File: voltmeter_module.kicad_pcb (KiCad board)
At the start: 2 copper layers, 16 parts, among them K1 EE2-3NUX, Q1 2N7002, U1 REF5030AD, U2 TL072, U3 MCP3561RT-E_ST, U5 ISO7762FDW, U6 NCS21802DMR2G, U7 CD4051B

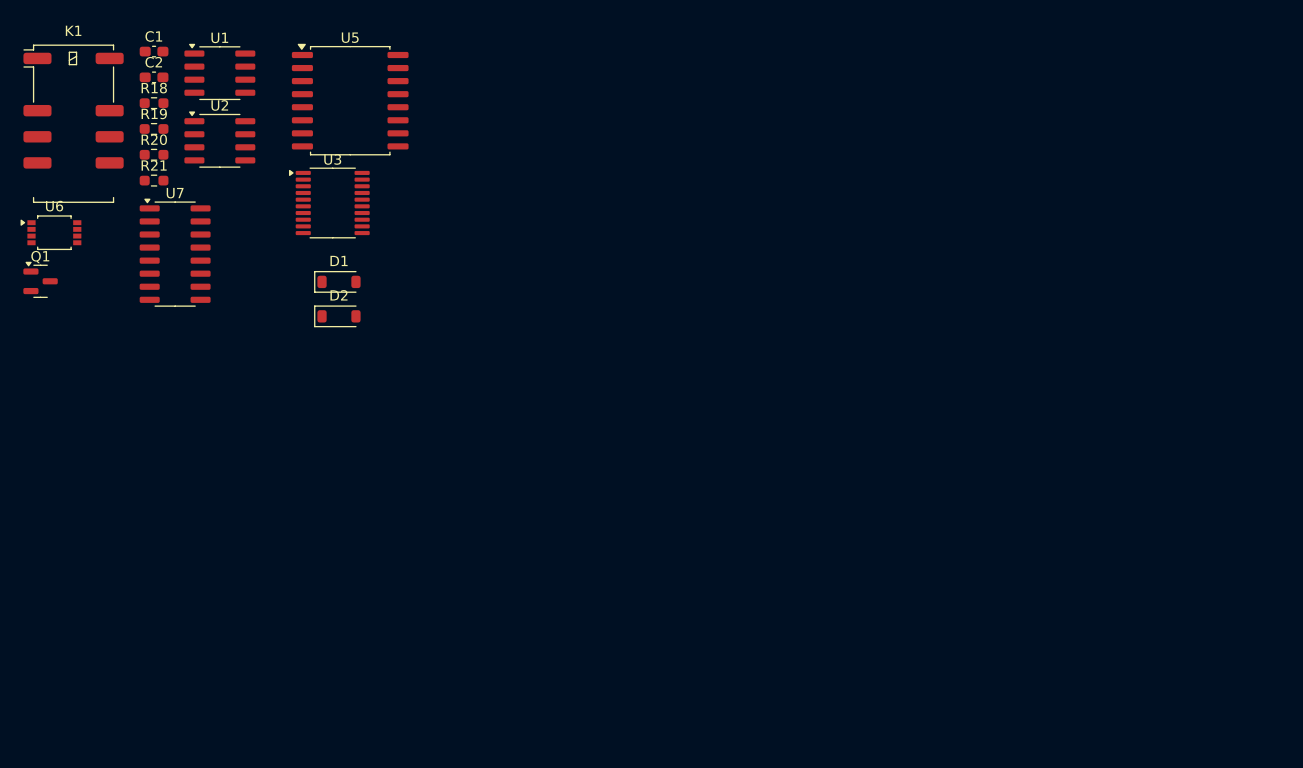
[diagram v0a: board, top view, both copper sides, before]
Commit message: Bootstraped input buffer.
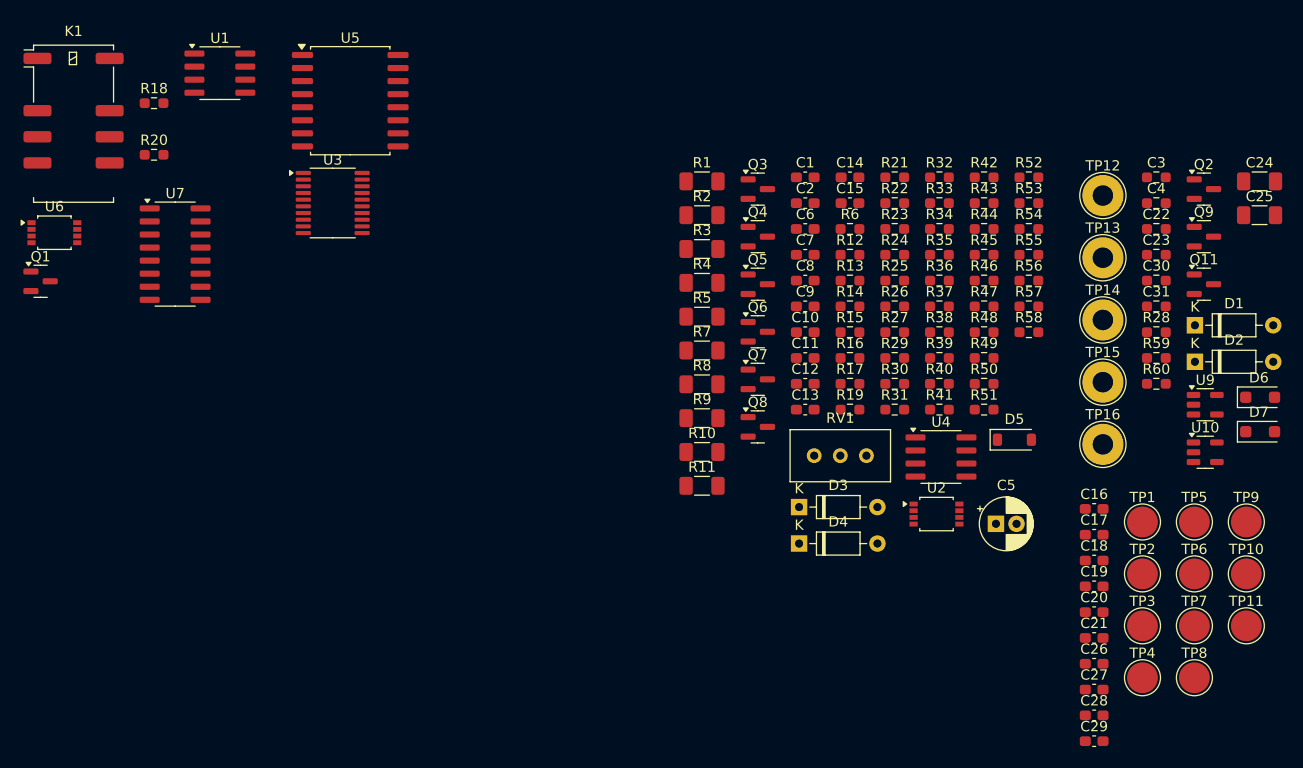
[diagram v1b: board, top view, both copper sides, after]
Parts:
- added C10: 100n, Capacitor_SMD:C_0603_1608Metric_Pad1.08x0.95mm_HandSolder, F.Cu at (184.2, 84.2)
- added C11: 1u, Capacitor_SMD:C_0603_1608Metric_Pad1.08x0.95mm_HandSolder, F.Cu at (184.2, 86.8)
- added C12: 1u, Capacitor_SMD:C_0603_1608Metric_Pad1.08x0.95mm_HandSolder, F.Cu at (184.2, 89.3)
- added C13: 100n, Capacitor_SMD:C_0603_1608Metric_Pad1.08x0.95mm_HandSolder, F.Cu at (184.2, 91.8)
- added C14: 100n, Capacitor_SMD:C_0603_1608Metric_Pad1.08x0.95mm_HandSolder, F.Cu at (188.6, 69.2)
- added C15: 100n, Capacitor_SMD:C_0603_1608Metric_Pad1.08x0.95mm_HandSolder, F.Cu at (188.6, 71.7)
- added C16: 100n, Capacitor_SMD:C_0603_1608Metric_Pad1.08x0.95mm_HandSolder, F.Cu at (212.3, 101.4)
- added C17: 100n, Capacitor_SMD:C_0603_1608Metric_Pad1.08x0.95mm_HandSolder, F.Cu at (212.3, 103.9)
- added C18: 1u, Capacitor_SMD:C_0603_1608Metric_Pad1.08x0.95mm_HandSolder, F.Cu at (212.3, 106.5)
- added C19: 1u, Capacitor_SMD:C_0603_1608Metric_Pad1.08x0.95mm_HandSolder, F.Cu at (212.3, 109.0)
- added C20: 1u, Capacitor_SMD:C_0603_1608Metric_Pad1.08x0.95mm_HandSolder, F.Cu at (212.3, 111.5)
- added C21: 100n, Capacitor_SMD:C_0603_1608Metric_Pad1.08x0.95mm_HandSolder, F.Cu at (212.3, 114.0)
- added C22: 220n, Resistor_SMD:R_0603_1608Metric_Pad0.98x0.95mm_HandSolder, F.Cu at (218.3, 74.2)
- added C23: 220n, Resistor_SMD:R_0603_1608Metric_Pad0.98x0.95mm_HandSolder, F.Cu at (218.3, 76.7)
- added C24: 2u2, Resistor_SMD:R_1206_3216Metric_Pad1.30x1.75mm_HandSolder, F.Cu at (228.4, 69.6)
- added C25: 2u2, Resistor_SMD:R_1206_3216Metric_Pad1.30x1.75mm_HandSolder, F.Cu at (228.4, 72.9)
- added C26: 1u, Capacitor_SMD:C_0603_1608Metric_Pad1.08x0.95mm_HandSolder, F.Cu at (212.3, 116.5)
- added C27: 100n, Capacitor_SMD:C_0603_1608Metric_Pad1.08x0.95mm_HandSolder, F.Cu at (212.3, 119.0)
- added C28: 1u, Capacitor_SMD:C_0603_1608Metric_Pad1.08x0.95mm_HandSolder, F.Cu at (212.3, 121.5)
- added C29: 100n, Capacitor_SMD:C_0603_1608Metric_Pad1.08x0.95mm_HandSolder, F.Cu at (212.3, 124.0)
- added C3: 1u, Resistor_SMD:R_0603_1608Metric_Pad0.98x0.95mm_HandSolder, F.Cu at (218.3, 69.2)
- added C30: 1u, Resistor_SMD:R_0603_1608Metric_Pad0.98x0.95mm_HandSolder, F.Cu at (218.3, 79.2)
- added C31: 1u, Resistor_SMD:R_0603_1608Metric_Pad0.98x0.95mm_HandSolder, F.Cu at (218.3, 81.7)
- added C4: 1u, Resistor_SMD:R_0603_1608Metric_Pad0.98x0.95mm_HandSolder, F.Cu at (218.3, 71.7)
- added C5: 47u, Capacitor_THT:CP_Radial_D5.0mm_P2.00mm, F.Cu at (202.7, 102.9)
- added C6: 100n, Capacitor_SMD:C_0603_1608Metric_Pad1.08x0.95mm_HandSolder, F.Cu at (184.2, 74.2)
- added C7: 100n, Capacitor_SMD:C_0603_1608Metric_Pad1.08x0.95mm_HandSolder, F.Cu at (184.2, 76.7)
- added C8: 100n, Capacitor_SMD:C_0603_1608Metric_Pad1.08x0.95mm_HandSolder, F.Cu at (184.2, 79.2)
- added C9: 100n, Capacitor_SMD:C_0603_1608Metric_Pad1.08x0.95mm_HandSolder, F.Cu at (184.2, 81.7)
- added D3: ZF2V4, Diode_THT:D_DO-35_SOD27_P7.62mm_Horizontal, F.Cu at (183.6, 101.2)
- added D4: ZF2V4, Diode_THT:D_DO-35_SOD27_P7.62mm_Horizontal, F.Cu at (183.6, 104.8)
- added D5: BAT48ZFILM, Diode_SMD:D_SOD-123, F.Cu at (204.5, 94.7)
- added D6: BZT52H-C16,115, Diode_SMD:D_SOD-123F, F.Cu at (228.4, 90.6)
- added D7: BZT52H-C16,115, Diode_SMD:D_SOD-123F, F.Cu at (228.4, 93.9)
- added Q11: MMBT3906, Package_TO_SOT_SMD:SOT-23, F.Cu at (223.0, 79.6)
- added Q2: MMBT3904, Package_TO_SOT_SMD:SOT-23, F.Cu at (223.0, 70.3)
- added Q3: MMBT3904, Package_TO_SOT_SMD:SOT-23, F.Cu at (179.6, 70.3)
- added Q4: MMBT3906, Package_TO_SOT_SMD:SOT-23, F.Cu at (179.6, 75.0)
- added Q5: MMBT3906, Package_TO_SOT_SMD:SOT-23, F.Cu at (179.6, 79.6)
- added Q6: MMBT3904, Package_TO_SOT_SMD:SOT-23, F.Cu at (179.6, 84.2)
- added Q7: MMBT3906, Package_TO_SOT_SMD:SOT-23, F.Cu at (179.6, 88.8)
- added Q8: MMBT3904, Package_TO_SOT_SMD:SOT-23, F.Cu at (179.6, 93.5)
- added Q9: MMBT3906, Package_TO_SOT_SMD:SOT-23, F.Cu at (223.0, 75.0)
- added R1: 1M, Resistor_SMD:R_1206_3216Metric_Pad1.30x1.75mm_HandSolder, F.Cu at (174.2, 69.6)
- added R10: 1M, Resistor_SMD:R_1206_3216Metric_Pad1.30x1.75mm_HandSolder, F.Cu at (174.2, 95.9)
- added R11: 1M, Resistor_SMD:R_1206_3216Metric_Pad1.30x1.75mm_HandSolder, F.Cu at (174.2, 99.2)
- added R12: 1k, Resistor_SMD:R_0603_1608Metric_Pad0.98x0.95mm_HandSolder, F.Cu at (188.6, 76.7)
- added R13: 100k, Resistor_SMD:R_0603_1608Metric_Pad0.98x0.95mm_HandSolder, F.Cu at (188.6, 79.2)
- added R14: 100, Resistor_SMD:R_0603_1608Metric_Pad0.98x0.95mm_HandSolder, F.Cu at (188.6, 81.7)
- added R15: 10, Resistor_SMD:R_0603_1608Metric_Pad0.98x0.95mm_HandSolder, F.Cu at (188.6, 84.2)
- added R16: 4k, Resistor_SMD:R_0603_1608Metric_Pad0.98x0.95mm_HandSolder, F.Cu at (188.6, 86.8)
- added R17: 2k, Resistor_SMD:R_0603_1608Metric_Pad0.98x0.95mm_HandSolder, F.Cu at (188.6, 89.3)
- added R2: 1M, Resistor_SMD:R_1206_3216Metric_Pad1.30x1.75mm_HandSolder, F.Cu at (174.2, 72.9)
- added R22: 100k, Resistor_SMD:R_0603_1608Metric_Pad0.98x0.95mm_HandSolder, F.Cu at (192.9, 71.7)
- added R23: 10k, Resistor_SMD:R_0603_1608Metric_Pad0.98x0.95mm_HandSolder, F.Cu at (192.9, 74.2)
- added R24: 1k, Resistor_SMD:R_0603_1608Metric_Pad0.98x0.95mm_HandSolder, F.Cu at (192.9, 76.7)
- added R25: 100k, Resistor_SMD:R_0603_1608Metric_Pad0.98x0.95mm_HandSolder, F.Cu at (192.9, 79.2)
- added R26: 1M, Resistor_SMD:R_0603_1608Metric_Pad0.98x0.95mm_HandSolder, F.Cu at (192.9, 81.7)
- added R27: 10M, Resistor_SMD:R_0603_1608Metric_Pad0.98x0.95mm_HandSolder, F.Cu at (192.9, 84.2)
- added R28: 22k, Resistor_SMD:R_0603_1608Metric_Pad0.98x0.95mm_HandSolder, F.Cu at (218.3, 84.2)
- added R29: 100k, Resistor_SMD:R_0603_1608Metric_Pad0.98x0.95mm_HandSolder, F.Cu at (192.9, 86.8)
- added R3: 1M, Resistor_SMD:R_1206_3216Metric_Pad1.30x1.75mm_HandSolder, F.Cu at (174.2, 76.2)
- added R30: 24.9k, Resistor_SMD:R_0603_1608Metric_Pad0.98x0.95mm_HandSolder, F.Cu at (192.9, 89.3)
- added R31: 1k, Resistor_SMD:R_0603_1608Metric_Pad0.98x0.95mm_HandSolder, F.Cu at (192.9, 91.8)
- added R32: 1k, Resistor_SMD:R_0603_1608Metric_Pad0.98x0.95mm_HandSolder, F.Cu at (197.2, 69.2)
- added R33: 4.7k, Resistor_SMD:R_0603_1608Metric_Pad0.98x0.95mm_HandSolder, F.Cu at (197.2, 71.7)
- added R34: 2k, Resistor_SMD:R_0603_1608Metric_Pad0.98x0.95mm_HandSolder, F.Cu at (197.2, 74.2)
- added R35: 1M, Resistor_SMD:R_0603_1608Metric_Pad0.98x0.95mm_HandSolder, F.Cu at (197.2, 76.7)
- added R36: 1M, Resistor_SMD:R_0603_1608Metric_Pad0.98x0.95mm_HandSolder, F.Cu at (197.2, 79.2)
- added R37: 10M, Resistor_SMD:R_0603_1608Metric_Pad0.98x0.95mm_HandSolder, F.Cu at (197.2, 81.7)
- added R38: 100M, Resistor_SMD:R_0603_1608Metric_Pad0.98x0.95mm_HandSolder, F.Cu at (197.2, 84.2)
- added R39: 10k, Resistor_SMD:R_0603_1608Metric_Pad0.98x0.95mm_HandSolder, F.Cu at (197.2, 86.8)
- added R4: 1M, Resistor_SMD:R_1206_3216Metric_Pad1.30x1.75mm_HandSolder, F.Cu at (174.2, 79.4)
- added R40: 10k, Resistor_SMD:R_0603_1608Metric_Pad0.98x0.95mm_HandSolder, F.Cu at (197.2, 89.3)
- added R41: 10k, Resistor_SMD:R_0603_1608Metric_Pad0.98x0.95mm_HandSolder, F.Cu at (197.2, 91.8)
- added R42: 10k, Resistor_SMD:R_0603_1608Metric_Pad0.98x0.95mm_HandSolder, F.Cu at (201.6, 69.2)
- added R43: 10k, Resistor_SMD:R_0603_1608Metric_Pad0.98x0.95mm_HandSolder, F.Cu at (201.6, 71.7)
- added R44: 10k, Resistor_SMD:R_0603_1608Metric_Pad0.98x0.95mm_HandSolder, F.Cu at (201.6, 74.2)
- added R45: 10k, Resistor_SMD:R_0603_1608Metric_Pad0.98x0.95mm_HandSolder, F.Cu at (201.6, 76.7)
- added R46: 2k, Resistor_SMD:R_0603_1608Metric_Pad0.98x0.95mm_HandSolder, F.Cu at (201.6, 79.2)
- added R47: 2k, Resistor_SMD:R_0603_1608Metric_Pad0.98x0.95mm_HandSolder, F.Cu at (201.6, 81.7)
- added R48: 2k, Resistor_SMD:R_0603_1608Metric_Pad0.98x0.95mm_HandSolder, F.Cu at (201.6, 84.2)
- added R49: 2k, Resistor_SMD:R_0603_1608Metric_Pad0.98x0.95mm_HandSolder, F.Cu at (201.6, 86.8)
- added R5: 1M, Resistor_SMD:R_1206_3216Metric_Pad1.30x1.75mm_HandSolder, F.Cu at (174.2, 82.7)
- added R50: 2k, Resistor_SMD:R_0603_1608Metric_Pad0.98x0.95mm_HandSolder, F.Cu at (201.6, 89.3)
- added R51: 4k, Resistor_SMD:R_0603_1608Metric_Pad0.98x0.95mm_HandSolder, F.Cu at (201.6, 91.8)
- added R52: 4k, Resistor_SMD:R_0603_1608Metric_Pad0.98x0.95mm_HandSolder, F.Cu at (205.9, 69.2)
- added R53: 10, Resistor_SMD:R_0603_1608Metric_Pad0.98x0.95mm_HandSolder, F.Cu at (205.9, 71.7)
- added R54: 100, Resistor_SMD:R_0603_1608Metric_Pad0.98x0.95mm_HandSolder, F.Cu at (205.9, 74.2)
- added R55: 100, Resistor_SMD:R_0603_1608Metric_Pad0.98x0.95mm_HandSolder, F.Cu at (205.9, 76.7)
- added R56: 470, Resistor_SMD:R_0603_1608Metric_Pad0.98x0.95mm_HandSolder, F.Cu at (205.9, 79.2)
- added R57: 470, Resistor_SMD:R_0603_1608Metric_Pad0.98x0.95mm_HandSolder, F.Cu at (205.9, 81.7)
- added R58: 100k, Resistor_SMD:R_0603_1608Metric_Pad0.98x0.95mm_HandSolder, F.Cu at (205.9, 84.2)
- added R59: 1k, Resistor_SMD:R_0603_1608Metric_Pad0.98x0.95mm_HandSolder, F.Cu at (218.3, 86.8)
- added R6: 10k, Resistor_SMD:R_0603_1608Metric_Pad0.98x0.95mm_HandSolder, F.Cu at (188.6, 74.2)
- added R60: 1k, Resistor_SMD:R_0603_1608Metric_Pad0.98x0.95mm_HandSolder, F.Cu at (218.3, 89.3)
- added R7: 1M, Resistor_SMD:R_1206_3216Metric_Pad1.30x1.75mm_HandSolder, F.Cu at (174.2, 86.0)
- added R8: 1M, Resistor_SMD:R_1206_3216Metric_Pad1.30x1.75mm_HandSolder, F.Cu at (174.2, 89.3)
- added R9: 1M, Resistor_SMD:R_1206_3216Metric_Pad1.30x1.75mm_HandSolder, F.Cu at (174.2, 92.6)
- added RV1: 10k, Potentiometer_THT:Potentiometer_Bourns_3296W_Vertical, F.Cu at (190.2, 96.2)
- added TP1: TestPoint, TestPoint:TestPoint_Pad_D3.0mm, F.Cu at (217.0, 102.7)
- added TP10: TestPoint, TestPoint:TestPoint_Pad_D3.0mm, F.Cu at (227.1, 107.8)
- added TP11: TestPoint, TestPoint:TestPoint_Pad_D3.0mm, F.Cu at (227.1, 112.8)
- added TP12: Vin+, TestPoint:TestPoint_THTPad_D4.0mm_Drill2.0mm, F.Cu at (213.2, 71.0)
- added TP13: Vin-, TestPoint:TestPoint_THTPad_D4.0mm_Drill2.0mm, F.Cu at (213.2, 77.0)
- added TP14: GND, TestPoint:TestPoint_THTPad_D4.0mm_Drill2.0mm, F.Cu at (213.2, 83.0)
- added TP15: GND_PC, TestPoint:TestPoint_THTPad_D4.0mm_Drill2.0mm, F.Cu at (213.2, 89.1)
- added TP16: 3V3_PC, TestPoint:TestPoint_THTPad_D4.0mm_Drill2.0mm, F.Cu at (213.2, 95.2)
- added TP2: TestPoint, TestPoint:TestPoint_Pad_D3.0mm, F.Cu at (217.0, 107.8)
- added TP3: TestPoint, TestPoint:TestPoint_Pad_D3.0mm, F.Cu at (217.0, 112.8)
- added TP4: TestPoint, TestPoint:TestPoint_Pad_D3.0mm, F.Cu at (217.0, 117.8)
- added TP5: TestPoint, TestPoint:TestPoint_Pad_D3.0mm, F.Cu at (222.1, 102.7)
- added TP6: TestPoint, TestPoint:TestPoint_Pad_D3.0mm, F.Cu at (222.1, 107.8)
- added TP7: TestPoint, TestPoint:TestPoint_Pad_D3.0mm, F.Cu at (222.1, 112.8)
- added TP8: TestPoint, TestPoint:TestPoint_Pad_D3.0mm, F.Cu at (222.1, 117.8)
- added TP9: TestPoint, TestPoint:TestPoint_Pad_D3.0mm, F.Cu at (227.1, 102.7)
- added U10: AP2204K-3.3, Package_TO_SOT_SMD:SOT-23-5, F.Cu at (223.1, 95.9)
- added U4: TL072, Package_SO:SOIC-8_3.9x4.9mm_P1.27mm, F.Cu at (197.4, 96.4)
- added U9: AP2204K-3.3, Package_TO_SOT_SMD:SOT-23-5, F.Cu at (223.1, 91.3)
- D1, D2: value 1N4148W -> ZF2V4; footprint Diode_SMD:D_SOD-123 -> Diode_THT:D_DO-35_SOD27_P7.62mm_Horizontal
- R18: value 8k -> 4k
- R19: value 8k -> 10k
- R20: value 1k -> 2k
- R21: value 1k -> 10k
- U2: value TL072 -> NCS21802DMR2G; footprint Package_SO:SOIC-8_3.9x4.9mm_P1.27mm -> Package_SO:OnSemi_Micro8
- moved D2 83.4 mm to (222.1, 87.1)
- moved D1 83.4 mm to (222.1, 83.6)
- moved U2 78.6 mm to (197.0, 101.9)
- moved R19 73.0 mm to (188.6, 91.8)
- moved R21 72.0 mm to (192.9, 69.2)
- moved C1 64.5 mm to (184.2, 69.2)
- moved C2 64.5 mm to (184.2, 71.7)
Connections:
- net /Digital section/~{CS} renamed CS
- net Net-(U2A--) renamed /Input stage/BUFFER_OUT
- net Net-(U3-SCK) renamed SCLK
- net Net-(U3-SDI) renamed MOSI
- net Net-(U3-SDO) renamed MISO
- C1 pad 1: INPUT- -> Net-(Q4-E)
- C1 pad 2: Net-(U6A-+) -> Net-(Q3-E)
- C2 pad 1: Net-(U6A--) -> INPUT-
- C2 pad 2: Net-(U6B-+) -> +3.3V
- D1 pad 1: +15V -> Net-(D1-K)
- D2 pad 1: -15V -> INPUT-
- D2 pad 2: Net-(D2-A) -> Net-(D1-K)
- K1 pad 5: Net-(K1-Pad5) -> unconnected-(K1-Pad5)
- K1 pad 8: unconnected-(K1-Pad8) -> Net-(K1-Pad8)
- R18 pad 1: Net-(U6A-+) -> Net-(R16-Pad2)
- R19 pad 1: Net-(U6A--) -> Net-(R19-Pad1)
- R19 pad 2: 1.5V_ref -> Net-(R19-Pad2)
- R20 pad 1: INPUT- -> Net-(R17-Pad2)
- R21 pad 1: Net-(U6B-+) -> Net-(R21-Pad1)
- R21 pad 2: Net-(U6A--) -> Net-(R21-Pad2)
- U1 pad 2: +3.3V -> +15.3V
- U1 pad 3: unconnected-(U1-Temp-Pad3) -> TEMP_SENSE
- U1 pad 5: unconnected-(U1-Trim/NR-Pad5) -> Net-(U1-Trim/NR)
- U2 pad 4: -15V -> Net-(Q4-E)
- U2 pad 6: 1.5V_ref -> Net-(U2B--)
- U2 pad 7: 1.5V_ref -> Net-(U2B--)
- U2 pad 8: +15V -> Net-(Q3-E)
- U3 pad 20: +3.3V -> +3.3V_D
- U5 pad 1: unconnected-(U5-Vcc1-Pad1) -> +3.3V_PC
- U5 pad 11: unconnected-(U5-INE-Pad11) -> TX
- U5 pad 12: unconnected-(U5-OUTD-Pad12) -> RX
- U5 pad 16: +3.3V -> +3.3V_D
- U5 pad 8: unconnected-(U5-GND1-Pad8) -> GND_PC
- U6 pad 1: Net-(U6B-+) -> /Digital section/3V_ref
- U6 pad 4: INPUT- -> -1V
- U6 pad 6: Net-(U6B--) -> 1.5V_ref
- U6 pad 7: /Digital section/3V_ref -> 1.5V_ref
- U7 pad 1: Net-(U7-X4) -> unconnected-(U7-X4-Pad1)
- U7 pad 12: Net-(U7-X3) -> unconnected-(U7-X3-Pad12)
- U7 pad 3: Net-(U6B--) -> Net-(U6A--)
- U7 pad 5: Net-(U7-X5) -> unconnected-(U7-X5-Pad5)
